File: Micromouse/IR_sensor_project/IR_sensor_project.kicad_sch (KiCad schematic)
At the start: 7 parts, among them J1 IR_1, Q1 SFH300, Q2 DMN3065LW-7

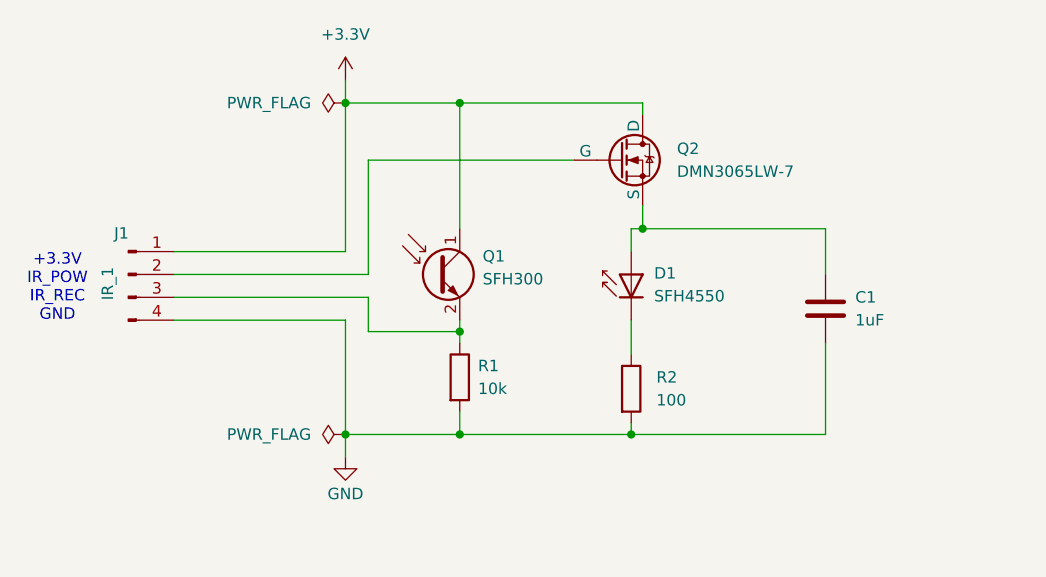
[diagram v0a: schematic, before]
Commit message: Completed IR board, ToF board, changed IMU
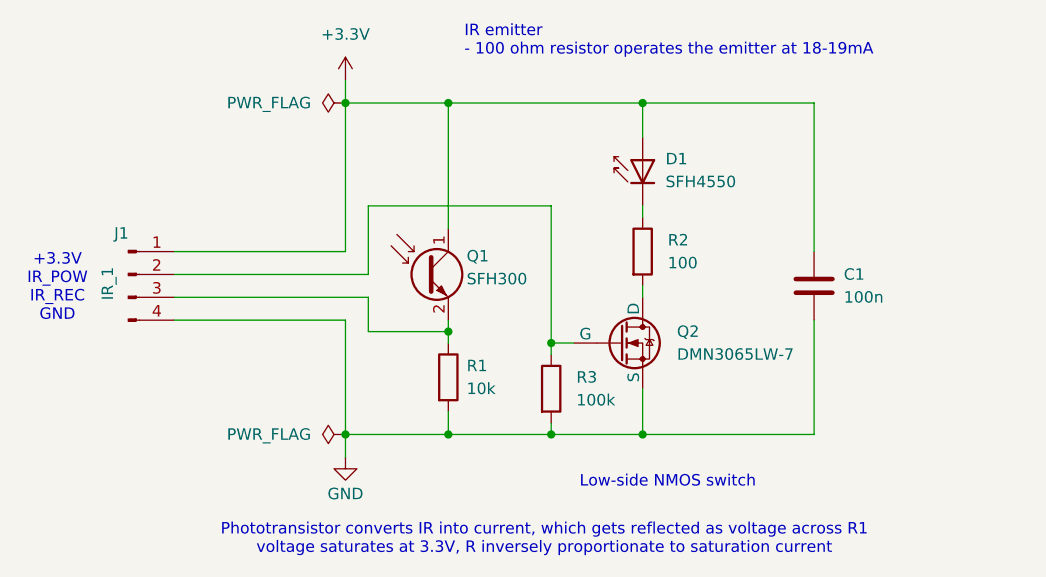
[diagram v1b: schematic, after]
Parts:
- added R3: 100k, Resistor_SMD:R_0603_1608Metric, symbol Device:R
- C1: value 1uF -> 100n
- J1: footprint Connector_JST:JST_ZH_B4B-ZR_1x04_P1.50mm_Vertical -> Connector_PinHeader_2.00mm:PinHeader_1x04_P2.00mm_Horizontal
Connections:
- net +3.3V: now also C1.1, D1.2 (A); no longer Q2.1 (D)
- net GND: now also Q2.3 (S), R3.2; no longer R2.2
- net at J1.2 (Pin_2), Q2.2 (G): now also R3.1
- new net: Q2.1 (D), R2.2
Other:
- note added: "IR emitter - 100 ohm resistor operates the emitter at 18-19mA"
- note added: "Low-side NMOS switch"
- note added: "Phototransistor converts IR into current, which gets reflected as voltage across R1 voltage saturates at 3.3V, R inversely proportionate to saturation current"
- moved on the sheet: D1, Q1, R1, R2
